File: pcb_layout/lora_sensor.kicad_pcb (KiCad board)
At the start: 2 copper layers, 73 parts, among them P1 USB_A, Q1 NXP BSS84, Q2 NXP 2N7002,215, Q3 NXP BSS84, U1 RN2483, U2 MCP73831/2, U3 TPS736, U4 PIC18F2XJ50, U5 BH1603FVC, U6 MCP9700T-E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

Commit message: Added PCB LAyout
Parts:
- added J1: CONN_01X01, Mounting_Holes:MountingHole_3.2mm_M3_Pad, F.Cu at (73.7, 115.6)
- added J2: CONN_01X01, Mounting_Holes:MountingHole_3.2mm_M3_Pad, F.Cu at (73.7, 74.9)
- added J3: CONN_01X01, Mounting_Holes:MountingHole_3.2mm_M3_Pad, F.Cu at (101.6, 97.8)
- Battery_Current1, Charge_Current1: footprint Socket_Strips:Socket_Strip_Straight_2x01_Pitch2.54mm -> Pin_Headers:Pin_Header_Straight_1x02_Pitch2.54mm
- Battery_Input1: footprint Socket_Strips:Socket_Strip_Straight_1x02_Pitch2.54mm -> Pin_Headers:Pin_Header_Angled_1x02_Pitch2.54mm
- C1, C10, C11, C13, C16, C2, C5, C6, C7, C8, C9, R1, R10, R11, R12, R13, R2, R5, R6, R8, U2, U3: moved to B.Cu
- MCU_Current1, RF_Current1: footprint Socket_Strips:Socket_Strip_Straight_1x02_Pitch2.54mm -> Pin_Headers:Pin_Header_Straight_1x02_Pitch2.54mm
- PICKIT1: footprint Socket_Strips:Socket_Strip_Straight_1x06_Pitch2.54mm -> Pin_Headers:Pin_Header_Straight_1x06_Pitch2.54mm
- UART2_CONN1: footprint Socket_Strips:Socket_Strip_Straight_1x03_Pitch2.54mm -> Pin_Headers:Pin_Header_Straight_1x03_Pitch2.54mm
- Y1: value 16Mhz -> FA_238; footprint Crystals:Crystal_SMD_EuroQuartz_MQ-4pin_7.0x5.0mm_HandSoldering -> libraries:Crystal_FA-238; moved to B.Cu
- moved D1 104.9 mm to (98.8, 106.7), turned to 180 degrees
- moved R3 97.0 mm to (72.4, 93.5), turned to 180 degrees
- moved R14 95.8 mm to (79.0, 79.2), turned to 180 degrees
- moved C2 95.4 mm to (74.9, 80.8), turned to 180 degrees
- moved R4 92.7 mm to (72.4, 91.4), turned to 180 degrees
- moved R26 89.7 mm to (96.5, 96.5), turned to 270 degrees
- moved C12 88.4 mm to (79.0, 75.2)
- moved R5 86.8 mm to (73.9, 83.1), turned to 270 degrees
- moved R6 86.7 mm to (73.9, 86.4), turned to 270 degrees
- moved C10 86.6 mm to (86.6, 97.8), turned to 180 degrees
- moved R2 85.7 mm to (75.9, 86.4), turned to 270 degrees
- moved Q2 82.7 mm to (83.8, 86.9), turned to 90 degrees
- moved R15 81.8 mm to (79.0, 77.2), turned to 180 degrees
- moved C17 77.5 mm to (100.3, 79.5), turned to 270 degrees
- moved Q3 76.6 mm to (94.0, 87.9), turned to 90 degrees
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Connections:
- PICKIT1 pad 2: Net-(PICKIT1-Pad2) -> (no net)
- PICKIT1 pad 5: /microcontroller/PGC -> /microcontroller/BUTTON_1
- PICKIT1 pad 6: Net-(PICKIT1-Pad6) -> (no net)
- U1 pad 10: Net-(U1-Pad10) -> (no net)
- U1 pad 13: Net-(U1-Pad13) -> (no net)
- U1 pad 14: Net-(U1-Pad14) -> (no net)
- U1 pad 15: Net-(U1-Pad15) -> (no net)
- U1 pad 16: Net-(U1-Pad16) -> (no net)
- U1 pad 17: Net-(U1-Pad17) -> (no net)
- U1 pad 18: Net-(U1-Pad18) -> (no net)
- U1 pad 19: Net-(U1-Pad19) -> (no net)
- U1 pad 2: Net-(U1-Pad2) -> (no net)
- U1 pad 29: Net-(U1-Pad29) -> (no net)
- U1 pad 3: Net-(U1-Pad3) -> (no net)
- U1 pad 30: Net-(U1-Pad30) -> (no net)
- U1 pad 31: Net-(U1-Pad31) -> (no net)
- U1 pad 39: Net-(U1-Pad39) -> (no net)
- U1 pad 4: Net-(U1-Pad4) -> (no net)
- U1 pad 40: Net-(U1-Pad40) -> (no net)
- U1 pad 42: Net-(U1-Pad42) -> (no net)
- U1 pad 43: Net-(U1-Pad43) -> (no net)
- U1 pad 44: Net-(U1-Pad44) -> (no net)
- U1 pad 45: Net-(U1-Pad45) -> (no net)
- U1 pad 46: Net-(U1-Pad46) -> (no net)
- U1 pad 5: Net-(U1-Pad5) -> (no net)
- U1 pad 9: Net-(U1-Pad9) -> (no net)
- U4 pad 27: /microcontroller/PGC -> /microcontroller/BUTTON_1
- U4 pad 4: /microcontroller/AN2_Ambient -> /microcontroller/AN3_Temperature
- U4 pad 5: /microcontroller/AN3_Temperature -> /microcontroller/AN2_Ambient
- U5 pad 4: Net-(U5-Pad4) -> (no net)
- U6 pad 1: Net-(U6-Pad1) -> (no net)
- U6 pad 5: Net-(U6-Pad5) -> (no net)
- Y1 pad 3: GND -> /microcontroller/OSC2
- Y1 pad 4: /microcontroller/OSC2 -> GND
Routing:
- net GND: track 0.00 -> 517.3 mm, vias 0 -> 35
- net /microcontroller/MCU_Power: track 0.00 -> 111.6 mm, vias 0 -> 6
- net /rf_section/RF_UART_TX: track 0.00 -> 76.9 mm, vias 0 -> 1
- net /rf_section/RF_UART_RX: track 0.00 -> 74.2 mm, vias 0 -> 1
- net /power_section/RF_Power: track 0.00 -> 67.3 mm, vias 0 -> 1
- net /microcontroller/BUTTON_1: track 0.00 -> 56.5 mm, vias 0 -> 4
- net /microcontroller/AN2_Ambient: track 0.00 -> 53.7 mm
- net /power_section/V_Battery: track 0.00 -> 43.2 mm
- net /microcontroller/LED3: track 0.00 -> 39.5 mm, vias 0 -> 2
- net /microcontroller/PGD: track 0.00 -> 36.3 mm, vias 0 -> 2
- net /microcontroller/LED2: track 0.00 -> 32.7 mm, vias 0 -> 2
- net /microcontroller/VB_Control: track 0.00 -> 28.3 mm, vias 0 -> 2
- net Net-(R15-Pad1): track 0.00 -> 28.2 mm, vias 0 -> 2
- net Net-(Q3-Pad3): track 0.00 -> 28.0 mm
- net /microcontroller/AN3_Temperature: track 0.00 -> 26.8 mm
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- added copper zone on B.Cu, net GND
- added copper zone on F.Cu, net GND
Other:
- net class Default: clearance 0.2 -> 0.18
- net class Power_trace added: clearance 0.3, trace_width 0.5, via_dia 0.6, via_drill 0.4
- net class RF_Traces added: clearance 0.25, trace_width 0.8, via_dia 0.6, via_drill 0.4
- rule trace_clearance: 0.2 -> 0.18
- rule via_min_drill: 0.3 -> 0.4

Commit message: Finalized layout, added gerbers and renders
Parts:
- removed RF_High1, RF_Low1: CONN_01X02, libraries:SMA_edge_connect
- added RF_HIGH_1: CONN_01X02, libraries:SMA_edge_connect, B.Cu at (111.8, 77.5)
- added RF_LOW_1: CONN_01X02, libraries:SMA_edge_connect, B.Cu at (111.8, 90.2)
- Battery_Input1: footprint Pin_Headers:Pin_Header_Angled_1x02_Pitch2.54mm -> Pin_Headers:Pin_Header_Straight_1x02_Pitch2.54mm
- Y1: value FA_238 -> FA_238 10MHz
- moved C1 2.17 mm to (106.2, 93.0), turned to 90 degrees
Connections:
- J1 pad 1: (no net) -> Net-(J1-Pad1)
- J2 pad 1: (no net) -> Net-(J2-Pad1)
- J3 pad 1: (no net) -> Net-(J3-Pad1)
- PICKIT1 pad 2: (no net) -> Net-(PICKIT1-Pad2)
- PICKIT1 pad 6: (no net) -> Net-(PICKIT1-Pad6)
- U1 pad 10: (no net) -> Net-(U1-Pad10)
- U1 pad 13: (no net) -> Net-(U1-Pad13)
- U1 pad 14: (no net) -> Net-(U1-Pad14)
- U1 pad 15: (no net) -> Net-(U1-Pad15)
- U1 pad 16: (no net) -> Net-(U1-Pad16)
- U1 pad 17: (no net) -> Net-(U1-Pad17)
- U1 pad 18: (no net) -> Net-(U1-Pad18)
- U1 pad 19: (no net) -> Net-(U1-Pad19)
- U1 pad 2: (no net) -> Net-(U1-Pad2)
- U1 pad 29: (no net) -> Net-(U1-Pad29)
- U1 pad 3: (no net) -> Net-(U1-Pad3)
- U1 pad 30: (no net) -> Net-(U1-Pad30)
- U1 pad 31: (no net) -> Net-(U1-Pad31)
- U1 pad 39: (no net) -> Net-(U1-Pad39)
- U1 pad 4: (no net) -> Net-(U1-Pad4)
- U1 pad 40: (no net) -> Net-(U1-Pad40)
- U1 pad 42: (no net) -> Net-(U1-Pad42)
- U1 pad 43: (no net) -> Net-(U1-Pad43)
- U1 pad 44: (no net) -> Net-(U1-Pad44)
- U1 pad 45: (no net) -> Net-(U1-Pad45)
- U1 pad 46: (no net) -> Net-(U1-Pad46)
- U1 pad 5: (no net) -> Net-(U1-Pad5)
- U1 pad 9: (no net) -> Net-(U1-Pad9)
- U5 pad 4: (no net) -> Net-(U5-Pad4)
- U6 pad 1: (no net) -> Net-(U6-Pad1)
- U6 pad 5: (no net) -> Net-(U6-Pad5)
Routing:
- net GND: track 517.3 -> 507.4 mm
- net /microcontroller/Sensors_Enable: track 19.1 -> 12.7 mm
- net /microcontroller/AN1_LDR: track 26.7 -> 24.6 mm
- net /microcontroller/RF_Reset: track 23.3 -> 25.3 mm
- net /microcontroller/MCU_Power: track 111.6 -> 112.5 mm
- net /power_section/RF_Power: track 67.3 -> 66.6 mm, vias 1 -> 3

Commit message: Small layout improvements
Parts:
- added G***: LOGO, libraries:oshw_all_no_com, F.Cu at (75.9, 84.7)
- Y1: value FA_238 10MHz -> FA_238
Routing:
- net (no net): track 0.51 -> 0.00 mm
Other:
- board outline added: 48.3 x 48.3 mm
- board text added: "LORA SENSOR NODE"
- board text added: "https://github.com/KolijnWolfaardt/TTN_sensor_node"
- board text added: "v 1.0"

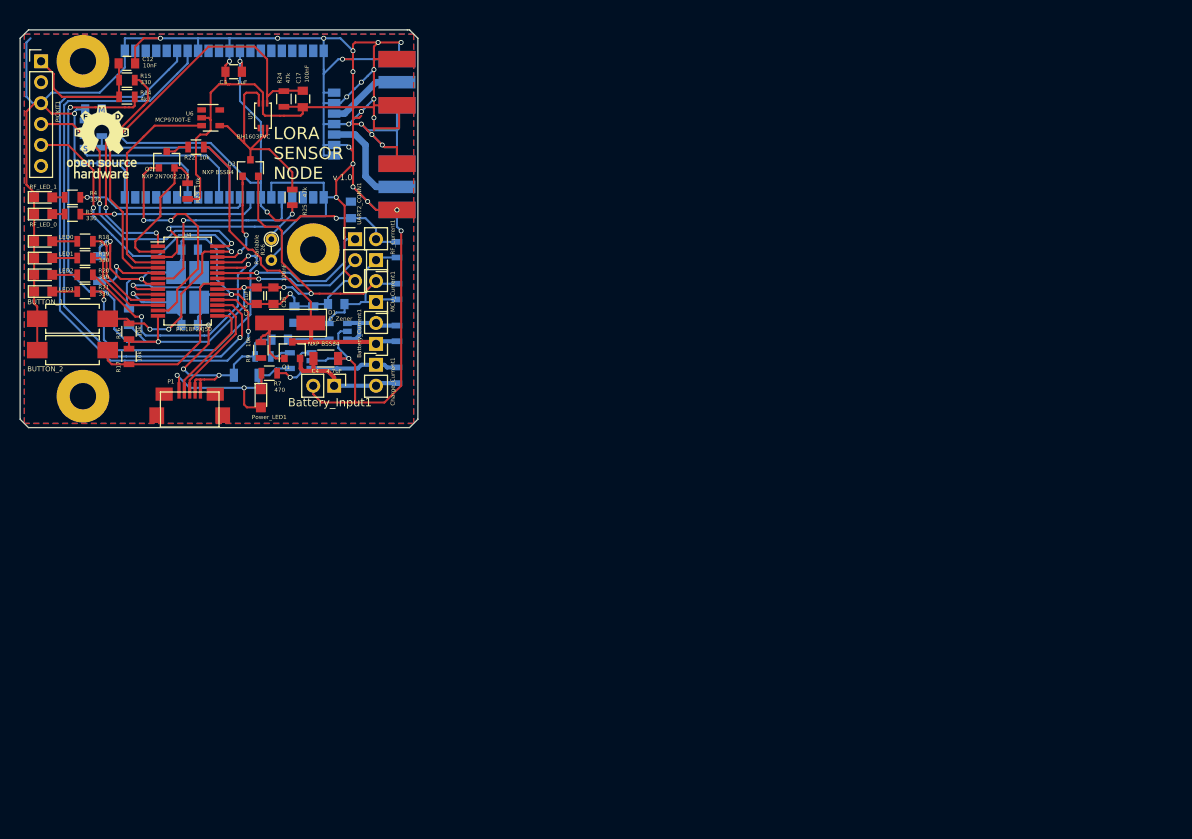
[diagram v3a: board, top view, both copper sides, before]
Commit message: More layout updates
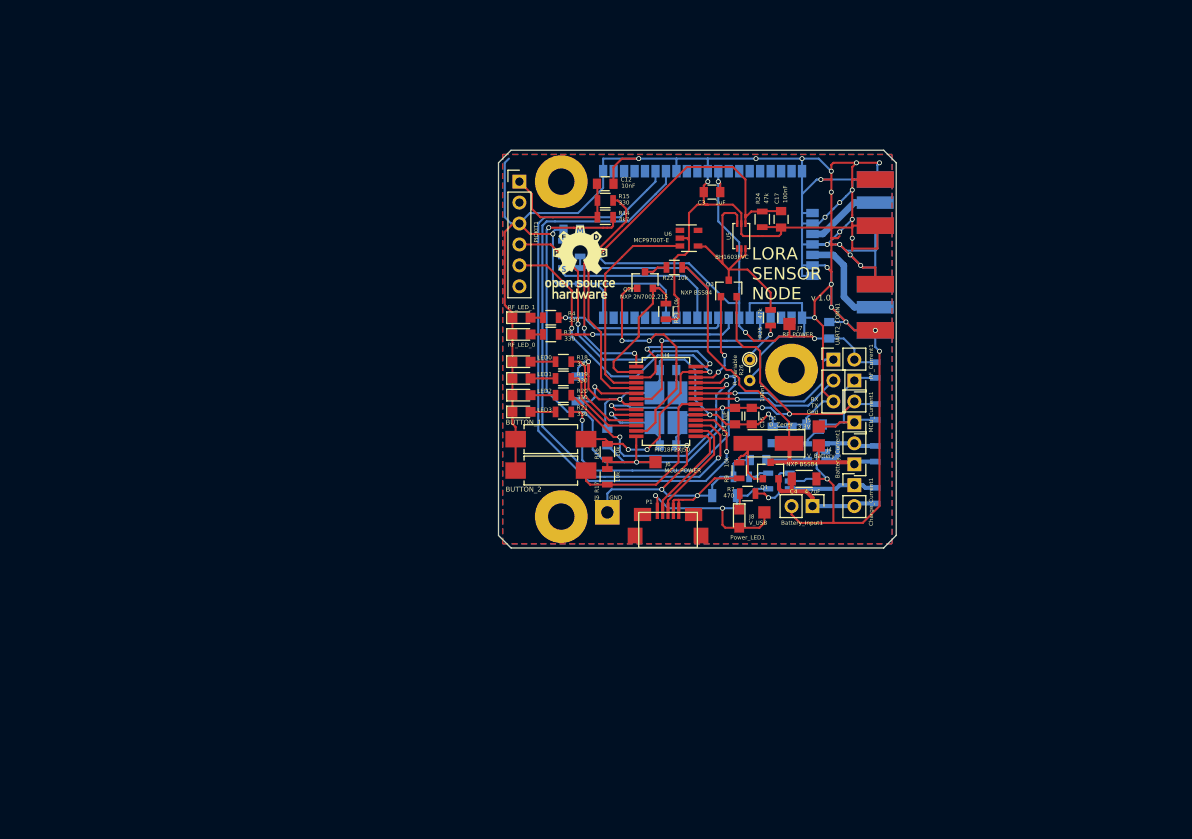
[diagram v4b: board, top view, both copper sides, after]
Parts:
- added J4: V_Battery, Measurement_Points:Measurement_Point_Square-SMD-Pad_Small, F.Cu at (162.9, 121.5)
- added J5: 3.3V, Measurement_Points:Measurement_Point_Square-SMD-Pad_Small, F.Cu at (162.9, 119.3)
- added J6: MCU_POWER, Measurement_Points:Measurement_Point_Square-SMD-Pad_Small, F.Cu at (143.1, 123.6)
- added J7: RF_POWER, Measurement_Points:Measurement_Point_Square-SMD-Pad_Small, F.Cu at (159.4, 106.8)
- added J8: V_USB, Measurement_Points:Measurement_Point_Square-SMD-Pad_Small, F.Cu at (156.3, 129.7)
- added J9: GND, Measurement_Points:Measurement_Point_Square-TH_Big, F.Cu at (137.3, 129.7)
- moved C1 59.8 mm to (164.2, 107.6)
- moved C7 59.8 mm to (157.4, 120.3)
- moved C9 59.8 mm to (159.6, 120.3)
- moved J1 59.8 mm to (131.7, 130.2)
- moved Q2 59.8 mm to (141.9, 101.5)
- moved R2 59.8 mm to (134.0, 101.0)
- moved U2 59.8 mm to (158.1, 125.9)
- moved U3 59.8 mm to (162.7, 122.3)
- moved U6 59.8 mm to (147.2, 96.4)
- moved C4 59.8 mm to (161.2, 125.6)
- moved G*** 59.8 mm to (134.0, 99.3)
- moved J2 59.8 mm to (131.7, 89.5)
- moved J3 59.8 mm to (159.6, 112.4)
- moved R1 59.8 mm to (134.0, 97.7)
- moved BUTTON_1 59.8 mm to (130.4, 120.8)
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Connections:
- J1 pad 1: Net-(J1-Pad1) -> (no net)
- J2 pad 1: Net-(J2-Pad1) -> (no net)
- J3 pad 1: Net-(J3-Pad1) -> (no net)
- PICKIT1 pad 2: Net-(PICKIT1-Pad2) -> (no net)
- PICKIT1 pad 6: Net-(PICKIT1-Pad6) -> (no net)
- U1 pad 10: Net-(U1-Pad10) -> (no net)
- U1 pad 13: Net-(U1-Pad13) -> (no net)
- U1 pad 14: Net-(U1-Pad14) -> (no net)
- U1 pad 15: Net-(U1-Pad15) -> (no net)
- U1 pad 16: Net-(U1-Pad16) -> (no net)
- U1 pad 17: Net-(U1-Pad17) -> (no net)
- U1 pad 18: Net-(U1-Pad18) -> (no net)
- U1 pad 19: Net-(U1-Pad19) -> (no net)
- U1 pad 2: Net-(U1-Pad2) -> (no net)
- U1 pad 29: Net-(U1-Pad29) -> (no net)
- U1 pad 3: Net-(U1-Pad3) -> (no net)
- U1 pad 30: Net-(U1-Pad30) -> (no net)
- U1 pad 31: Net-(U1-Pad31) -> (no net)
- U1 pad 39: Net-(U1-Pad39) -> (no net)
- U1 pad 4: Net-(U1-Pad4) -> (no net)
- U1 pad 40: Net-(U1-Pad40) -> (no net)
- U1 pad 42: Net-(U1-Pad42) -> (no net)
- U1 pad 43: Net-(U1-Pad43) -> (no net)
- U1 pad 44: Net-(U1-Pad44) -> (no net)
- U1 pad 45: Net-(U1-Pad45) -> (no net)
- U1 pad 46: Net-(U1-Pad46) -> (no net)
- U1 pad 5: Net-(U1-Pad5) -> (no net)
- U1 pad 9: Net-(U1-Pad9) -> (no net)
- U5 pad 4: Net-(U5-Pad4) -> (no net)
- U6 pad 1: Net-(U6-Pad1) -> (no net)
- U6 pad 5: Net-(U6-Pad5) -> (no net)
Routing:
- net GND: track 507.4 -> 524.5 mm
- net /microcontroller/V_USB: track 22.2 -> 26.7 mm
- net +3V3: track 23.2 -> 27.7 mm
- net /microcontroller/MCU_Power: track 112.5 -> 114.7 mm
- net /power_section/V_Battery: track 43.5 -> 45.5 mm
- net /power_section/RF_Power: track 66.6 -> 68.1 mm
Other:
- outline, holes or cut-outs redrawn
- board text added: "Gnd"
- board text added: "RX"
- board text added: "TX"

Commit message: Manufactured version
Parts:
- removed G***: LOGO, libraries:oshw_all_no_com
- removed Power_LED1: LED, LEDs:LED_0805
- added Charge_LED1: LED, LEDs:LED_0805, F.Cu at (153.3, 130.7)
